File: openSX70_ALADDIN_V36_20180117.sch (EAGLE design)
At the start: 38 parts, among them Q1 5.8A/30V/35mΩ, Q2 5.8A/30V/35mΩ, U1 ATMEGA328P_TQFP, U3 BH1750FVI-TR, Y1 CSTCE16M0V53-R0

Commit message: changed version number and name on schematic
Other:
- note added: "GitHub "aladdin" version"
- note added: "v 3.6"
- note removed: "GitHub "cake" version"
- note removed: "v 3.5"
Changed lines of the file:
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@@
 or
 FLASH</text>
-<text x="246.38" y="2.54" size="2.1844" layer="97" align="center">v 3.5</text>
+<text x="246.38" y="2.54" size="2.1844" layer="97" align="center">v 3.6</text>
 <text x="203.454" y="24.638" size="2.0066" layer="97" align="center">Design by Joaquín de Prada
 Creative Commons "Attribution-NonCommercial 4.0 International (CC BY-NC 4.0)"
 https://creativecommons.org/licenses/by-nc/4.0/</text>
-<text x="171.196" y="1.016" size="3.81" layer="97">GitHub "cake" version</text>
+<text x="171.196" y="1.016" size="3.81" layer="97">GitHub "aladdin" version</text>
 <text x="129.54" y="40.64" size="1.6764" layer="97">DEFAULT 6V
 ONLY 6V OR 3.3V

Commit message: Added a protection diode D1 to solenoid#1 for protection. I had assumed that it was built in the solenoid but Phyvine Tong indicated that some later models (alpha) don't have it.
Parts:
- added D1: 1N4148WSF, zetex:DSOD323
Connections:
- net 6V: now also D1.C
- net SOL1-: now also D1.A
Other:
- note removed: "(DIODE IN SOLENOID)"
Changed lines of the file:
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@@
 <part name="JP1" library="SparkFun-Jumpers" deviceset="JUMPER-SMT_3_1-NC_TRACE" device="_SILK" value="FTDI VCC SELECTOR"/>
 <part name="P+7" library="openSX70" deviceset="VCC" device="" value="6V"/>
+<part name="D1" library="zetex" library_urn="urn:adsk.eagle:library:418" deviceset="D" device="SOD323" package3d_urn="urn:adsk.eagle:package:30992/1" value="1N4148WSF"/>
+<part name="P+8" library="openSX70" deviceset="VCC" device="" value="6V"/>
 </parts>
 <sheets>
@@
 <plain>
 <text x="35.56" y="111.76" size="1.6764" layer="91">1-WIRE</text>
-<text x="198.12" y="48.26" size="1.6764" layer="97" rot="R180">(DIODE IN
-SOLENOID)
-</text>
 <text x="15.24" y="137.16" size="2.1844" layer="91">FFA</text>
 <text x="76.2" y="139.7" size="2.1844" layer="97" align="center">LIGHT
@@
 </instance>
 <instance part="P+7" gate="VCC" x="137.16" y="53.34" rot="R270"/>
+<instance part="D1" gate="G$1" x="195.58" y="50.8" smashed="yes" rot="R180">
+<attribute name="NAME" x="195.58" y="47.625" size="1.778" layer="95" rot="R180"/>
+<attribute name="VALUE" x="190.5" y="53.975" size="1.778" layer="96"/>
+</instance>
+<instance part="P+8" gate="VCC" x="182.88" y="50.8" rot="R90"/>
 </instances>
 <busses>
@@
 <wire x1="134.62" y1="53.34" x2="132.08" y2="53.34" width="0.1524" layer="91"/>
 </segment>
+<segment>
+<pinref part="P+8" gate="VCC" pin="6V"/>
+<pinref part="D1" gate="G$1" pin="C"/>
+<wire x1="185.42" y1="50.8" x2="193.04" y2="50.8" width="0.1524" layer="91"/>
+</segment>
 </net>
 <net name="SOL1-" class="0">
@@
 <segment>
 <pinref part="SOL1" gate="G$1" pin="-"/>
-<wire x1="208.28" y1="50.8" x2="200.66" y2="50.8" width="0.1524" layer="91"/>
+<wire x1="208.28" y1="50.8" x2="203.2" y2="50.8" width="0.1524" layer="91"/>
 <label x="200.66" y="48.26" size="1.778" layer="95"/>
-</segment>
-</net>
+<pinref part="D1" gate="G$1" pin="A"/>
+<wire x1="203.2" y1="50.8" x2="200.66" y2="50.8" width="0.1524" layer="91"/>
+<wire x1="198.12" y1="50.8" x2="200.66" y2="50.8" width="0.1524" layer="91"/>
+</segment>
+</net>

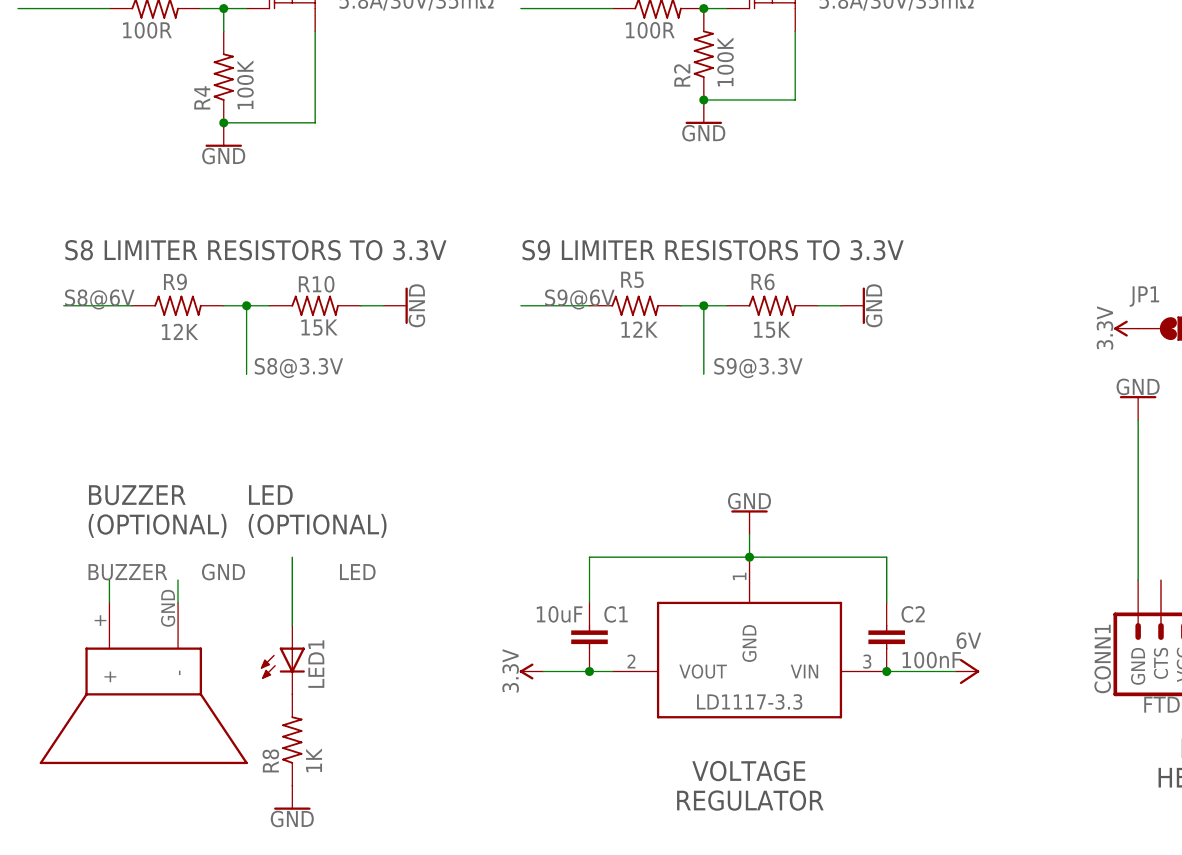
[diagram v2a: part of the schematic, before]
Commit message: Added GND 6V and 3.3V test points. Removed a bunch of innecessary vias.
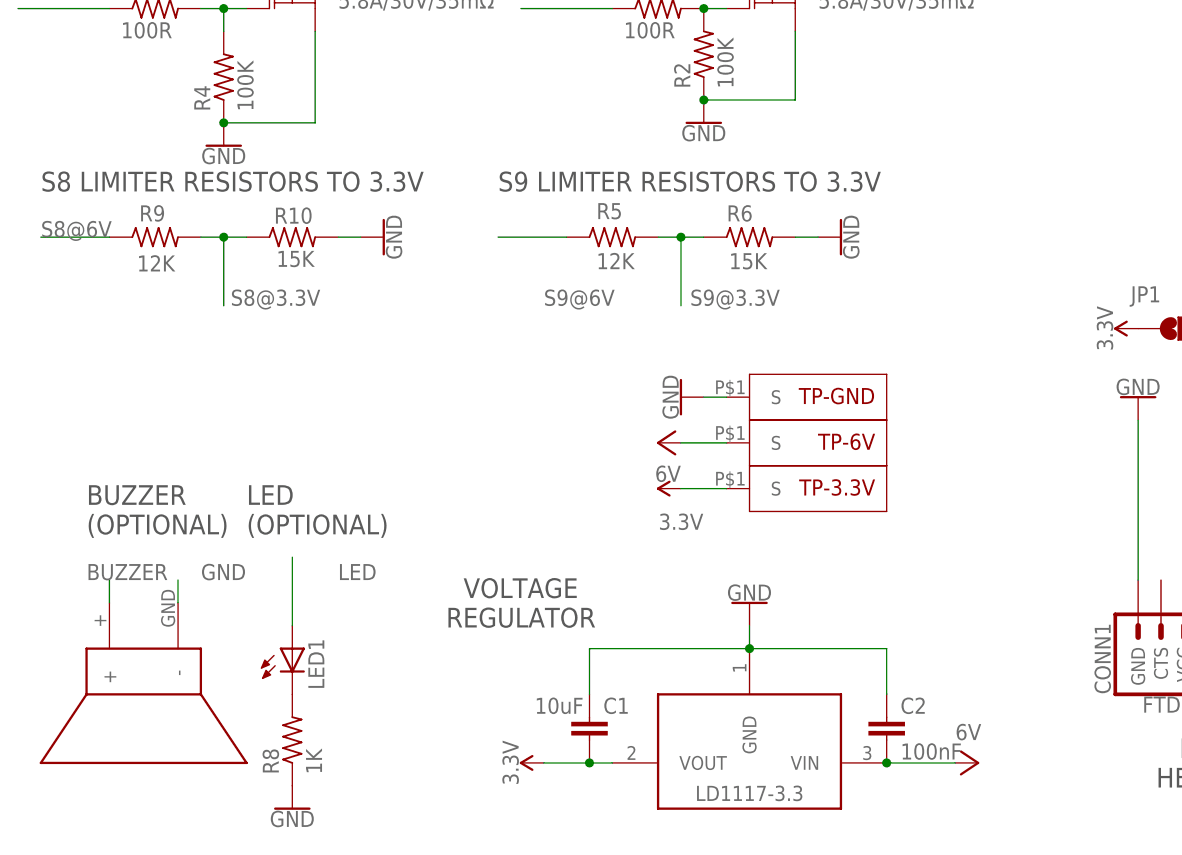
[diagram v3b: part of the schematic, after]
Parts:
- added TP-3.3V, TP-6V, TP-GND: SX70-S-PAD-NEW, openSX70:SX70-S-PAD-NEW
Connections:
- net 3.3V: now also TP-3.3V.S
- net 6V: now also TP-6V.S
- net GND: now also TP-GND.S
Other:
- moved on the sheet: C1, C2, R10, R5, R6, R9

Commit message: I keep on tweaking compulsively. Definitely have to stop.
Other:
- note added: "TP"
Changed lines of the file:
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@@
 NOT BOTH AT ONCE
 </text>
+<text x="63.5" y="40.64" size="2.1844" layer="97" align="center">TP</text>
 </plain>
 <instances>

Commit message: Added TP to pins 15 16 and 17, for bootloader programming (?)
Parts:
- added TP15, TP16, TP17: PTR1TP08R, testpad:PTR1TP08R
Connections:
- net LED: now also TP17.TP
- net S1: now also TP16.TP
- net SOL2: now also TP15.TP
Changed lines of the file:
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@@
 <part name="P+9" library="openSX70" deviceset="VCC" device="" value="6V"/>
 <part name="GND4" library="SparkFun-PowerSymbols" library_urn="urn:adsk.eagle:library:530" deviceset="GND" device=""/>
+<part name="TP15" library="testpad" library_urn="urn:adsk.eagle:library:385" deviceset="PTR1" device="TP08R" package3d_urn="urn:adsk.eagle:package:27956/1" value="PTR1TP08R"/>
+<part name="TP16" library="testpad" library_urn="urn:adsk.eagle:library:385" deviceset="PTR1" device="TP08R" package3d_urn="urn:adsk.eagle:package:27956/1" value="PTR1TP08R"/>
+<part name="TP17" library="testpad" library_urn="urn:adsk.eagle:library:385" deviceset="PTR1" device="TP08R" package3d_urn="urn:adsk.eagle:package:27956/1" value="PTR1TP08R"/>
 </parts>
 <sheets>
@@
 <attribute name="VALUE" x="70.866" y="45.72" size="1.778" layer="96" rot="R270" align="top-center"/>
 </instance>
+<instance part="TP15" gate="G$1" x="208.28" y="73.66" smashed="yes" rot="R90">
+<attribute name="NAME" x="220.98" y="74.676" size="1.778" layer="95" rot="R180"/>
+<attribute name="TP_SIGNAL_NAME" x="210.82" y="74.93" size="1.778" layer="97" rot="R90"/>
+</instance>
+<instance part="TP16" gate="G$1" x="208.28" y="71.12" smashed="yes" rot="R90">
+<attribute name="NAME" x="220.98" y="71.882" size="1.778" layer="95" rot="R180"/>
+<attribute name="TP_SIGNAL_NAME" x="210.82" y="72.39" size="1.778" layer="97" rot="R90"/>
+</instance>
+<instance part="TP17" gate="G$1" x="208.28" y="68.58" smashed="yes" rot="R90">
+<attribute name="NAME" x="220.98" y="69.342" size="1.778" layer="95" rot="R180"/>
+<attribute name="TP_SIGNAL_NAME" x="210.82" y="69.85" size="1.778" layer="97" rot="R90"/>
+</instance>
 </instances>
 <busses>
@@
 <segment>
 <pinref part="U1" gate="U$1" pin="PB4(MISO)"/>
-<wire x1="193.04" y1="71.12" x2="200.66" y2="71.12" width="0.1524" layer="91"/>
+<wire x1="193.04" y1="71.12" x2="205.74" y2="71.12" width="0.1524" layer="91"/>
 <label x="195.58" y="71.12" size="1.778" layer="95"/>
+<pinref part="TP16" gate="G$1" pin="TP"/>
 </segment>
 <segment>
@@
 <segment>
 <pinref part="U1" gate="U$1" pin="PB5(SCK)"/>
-<wire x1="193.04" y1="68.58" x2="200.66" y2="68.58" width="0.1524" layer="91"/>
+<wire x1="193.04" y1="68.58" x2="205.74" y2="68.58" width="0.1524" layer="91"/>
 <label x="195.58" y="68.58" size="1.778" layer="95"/>
+<pinref part="TP17" gate="G$1" pin="TP"/>
 </segment>
 <segment>
@@
 <segment>
 <pinref part="U1" gate="U$1" pin="PB3(MOSI/OC2)"/>
-<wire x1="193.04" y1="73.66" x2="200.66" y2="73.66" width="0.1524" layer="91"/>
+<wire x1="193.04" y1="73.66" x2="205.74" y2="73.66" width="0.1524" layer="91"/>
 <label x="195.58" y="73.66" size="1.778" layer="95"/>
-</segment>
-<segment>
+<pinref part="TP15" gate="G$1" pin="TP"/>
+</segment>
+<segment>

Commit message: Minor changes, also added TP SCL and SDA. Created gerbers.
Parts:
- added TP-SCL, TP-SDA: PTR1TP08R, testpad:PTR1TP08R
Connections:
- net SCL: now also TP-SCL.TP
- net SDA: now also TP-SDA.TP
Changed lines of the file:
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@@
 <part name="TP16" library="testpad" library_urn="urn:adsk.eagle:library:385" deviceset="PTR1" device="TP08R" package3d_urn="urn:adsk.eagle:package:27956/1" value="PTR1TP08R"/>
 <part name="TP17" library="testpad" library_urn="urn:adsk.eagle:library:385" deviceset="PTR1" device="TP08R" package3d_urn="urn:adsk.eagle:package:27956/1" value="PTR1TP08R"/>
+<part name="TP-SDA" library="testpad" library_urn="urn:adsk.eagle:library:385" deviceset="PTR1" device="TP08R" package3d_urn="urn:adsk.eagle:package:27956/1" value="PTR1TP08R"/>
+<part name="TP-SCL" library="testpad" library_urn="urn:adsk.eagle:library:385" deviceset="PTR1" device="TP08R" package3d_urn="urn:adsk.eagle:package:27956/1" value="PTR1TP08R"/>
 </parts>
 <sheets>
@@
 <attribute name="TP_SIGNAL_NAME" x="210.82" y="69.85" size="1.778" layer="97" rot="R90"/>
 </instance>
+<instance part="TP-SDA" gate="G$1" x="104.14" y="116.84" smashed="yes">
+<attribute name="NAME" x="105.156" y="99.06" size="1.778" layer="95" rot="R90"/>
+<attribute name="TP_SIGNAL_NAME" x="105.41" y="114.3" size="1.778" layer="97"/>
+</instance>
+<instance part="TP-SCL" gate="G$1" x="99.06" y="111.76" smashed="yes">
+<attribute name="NAME" x="100.076" y="96.52" size="1.778" layer="95" rot="R90"/>
+<attribute name="TP_SIGNAL_NAME" x="100.33" y="109.22" size="1.778" layer="97"/>
+</instance>
 </instances>
 <busses>
@@
 <pinref part="U3" gate="G$1" pin="SDA"/>
 <label x="104.14" y="121.92" size="1.778" layer="95"/>
-<wire x1="104.14" y1="129.54" x2="104.14" y2="124.46" width="0.1524" layer="91"/>
+<pinref part="TP-SDA" gate="G$1" pin="TP"/>
+<wire x1="104.14" y1="119.38" x2="104.14" y2="129.54" width="0.1524" layer="91"/>
 </segment>
 </net>
@@
 <segment>
 <pinref part="U3" gate="G$1" pin="SCL"/>
-<wire x1="99.06" y1="129.54" x2="99.06" y2="111.76" width="0.1524" layer="91"/>
+<wire x1="99.06" y1="129.54" x2="99.06" y2="114.3" width="0.1524" layer="91"/>
 <label x="93.98" y="111.76" size="1.778" layer="95"/>
-</segment>
-</net>
+<pinref part="TP-SCL" gate="G$1" pin="TP"/>
+</segment>
+</net>
